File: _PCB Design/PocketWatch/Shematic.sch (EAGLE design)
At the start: 57 parts, among them Q1 MMBTA56-SOT23, U2 ATTINY88-AU

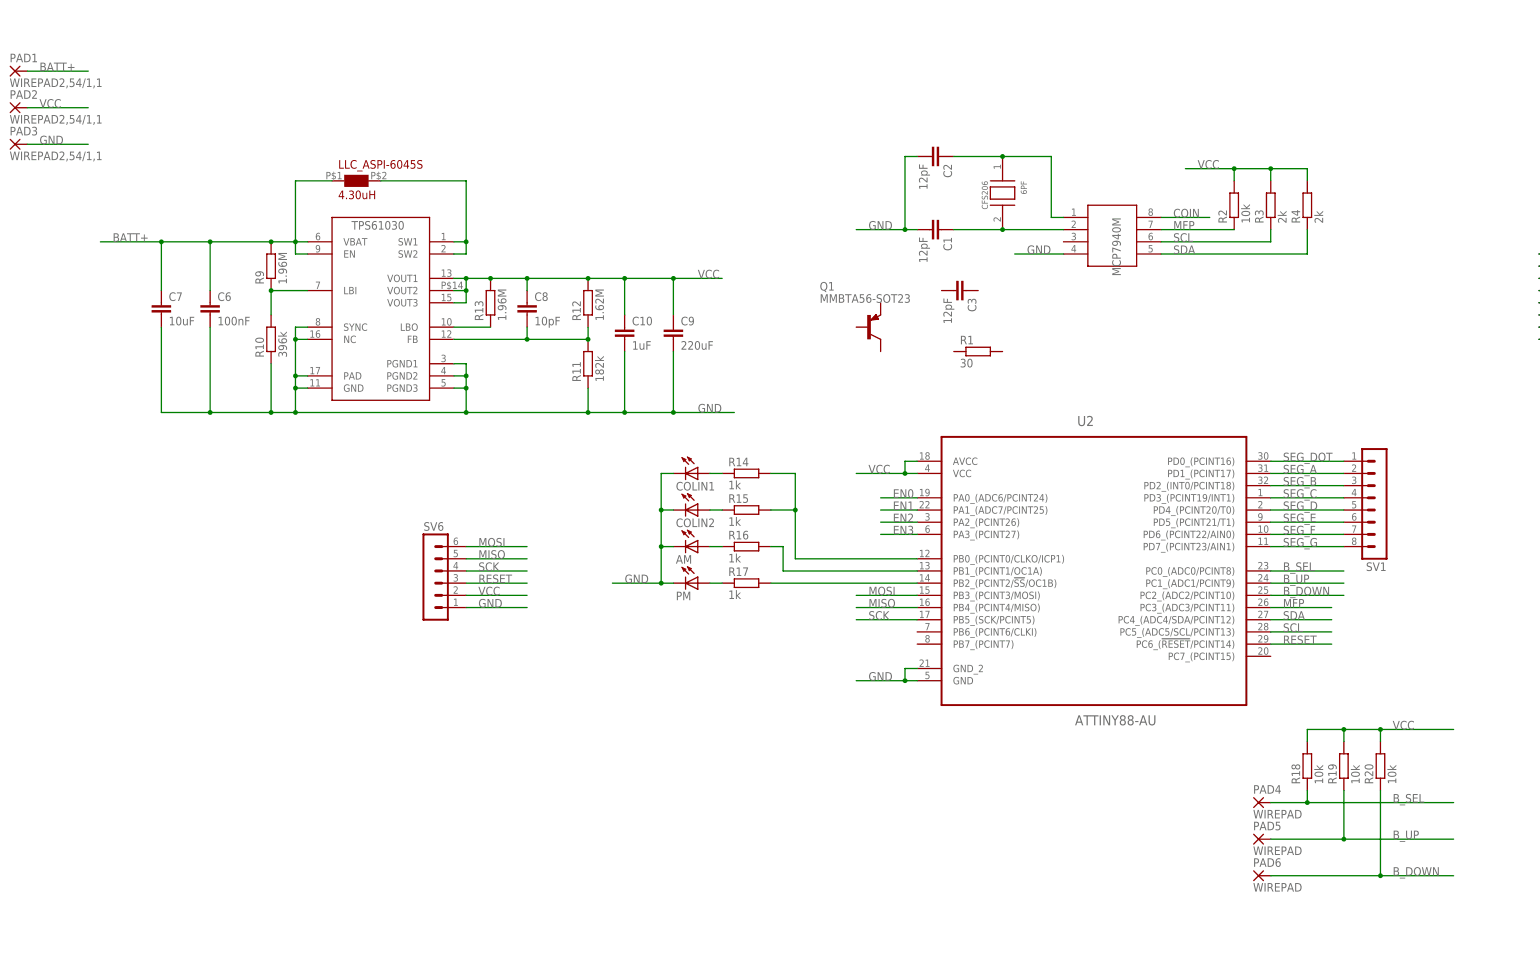
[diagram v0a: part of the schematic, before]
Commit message: Added Coin Cell
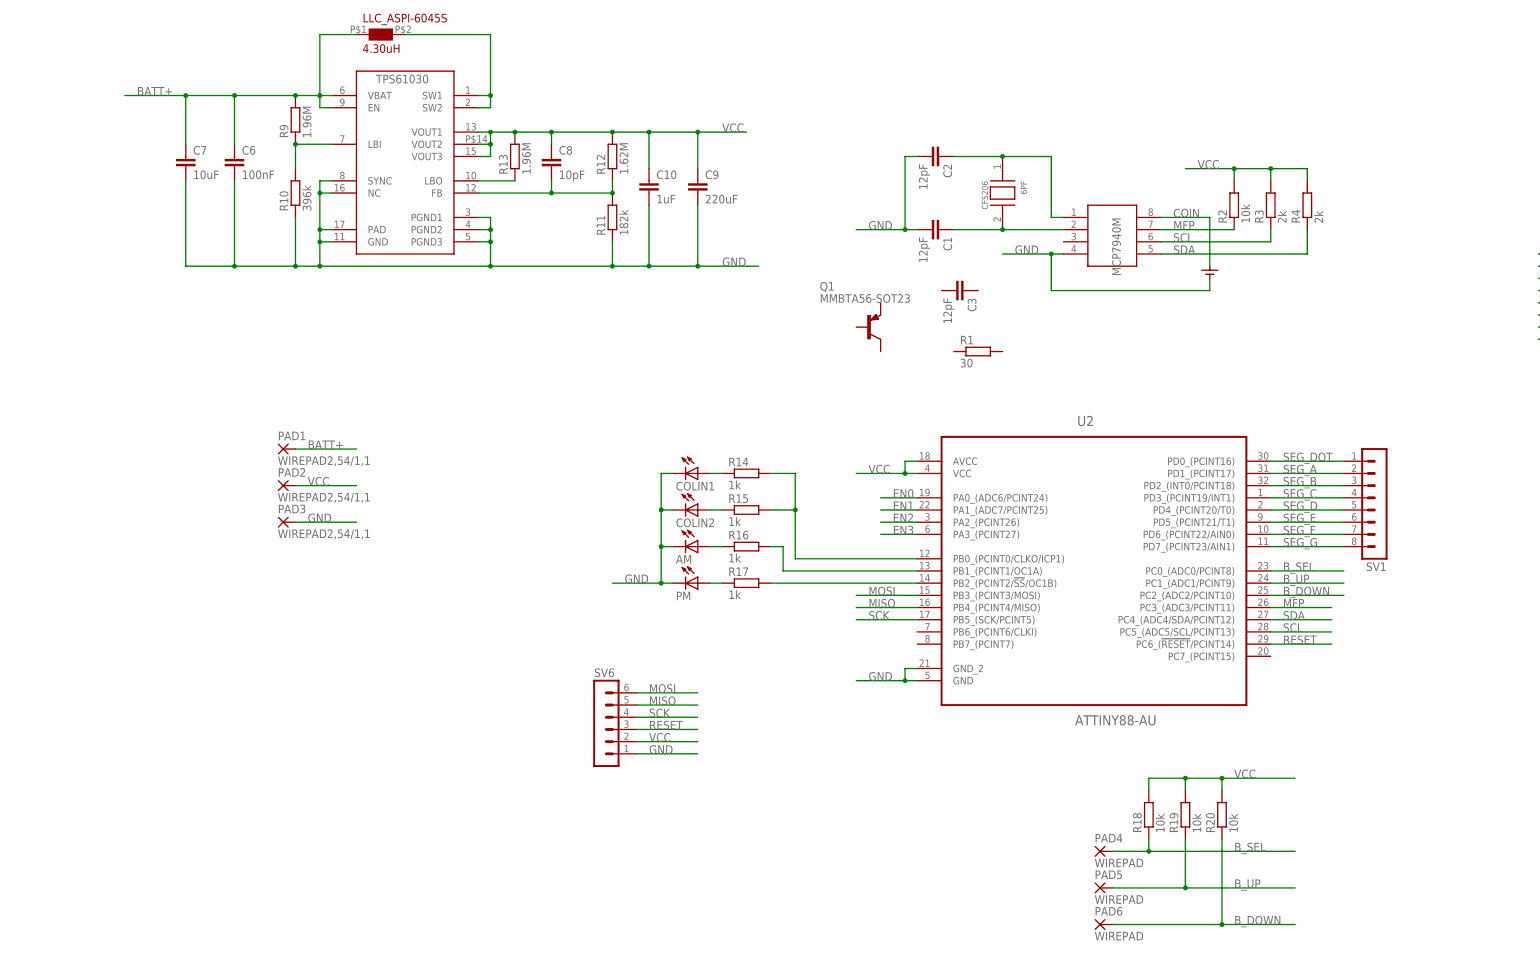
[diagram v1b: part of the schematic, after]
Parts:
- added U$5: COIN, Library:COIN
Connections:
- net COIN: now also U$5.V+
- net GND: now also U$5.V-
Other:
- moved on the sheet: C10, C6, C7, C8, C9, LLC_ASPI-6045S, PAD1, PAD2, PAD3, PAD4, PAD5, PAD6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

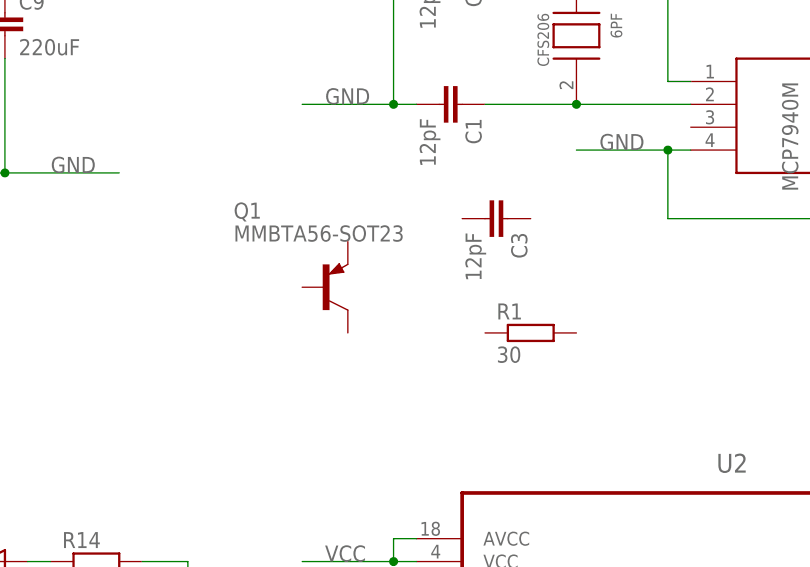
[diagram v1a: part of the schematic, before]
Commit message: Added board. Routed tubes sub-board. Fixed remaining schematic issues.
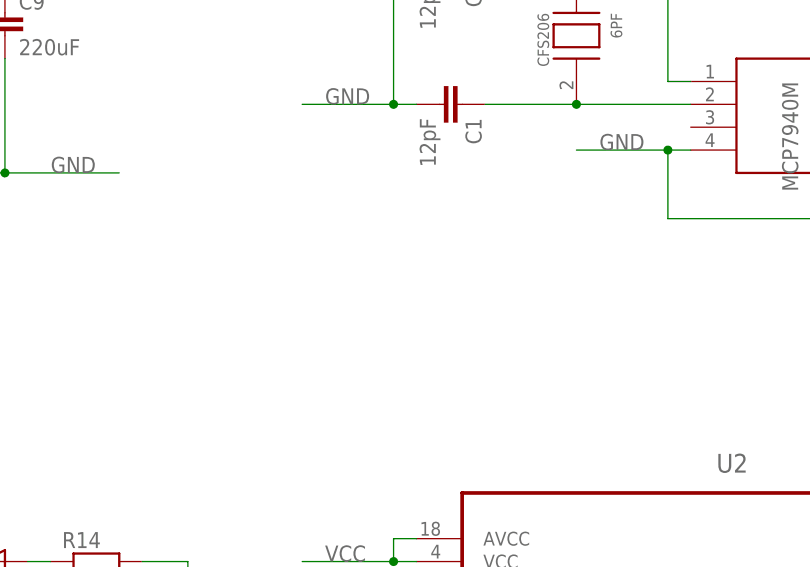
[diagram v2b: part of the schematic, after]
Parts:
- removed C3: 12pF, eagle-ltspice:CC1206
- removed Q1: MMBTA56-SOT23, transistor-pnp:MMBTA56-SOT23
- removed R1: 30, eagle-ltspice:RR1206
- renumbered U$1 to TUBE3, U$2 to TUBE2, U$3 to TUBE0, U$4 to TUBE1

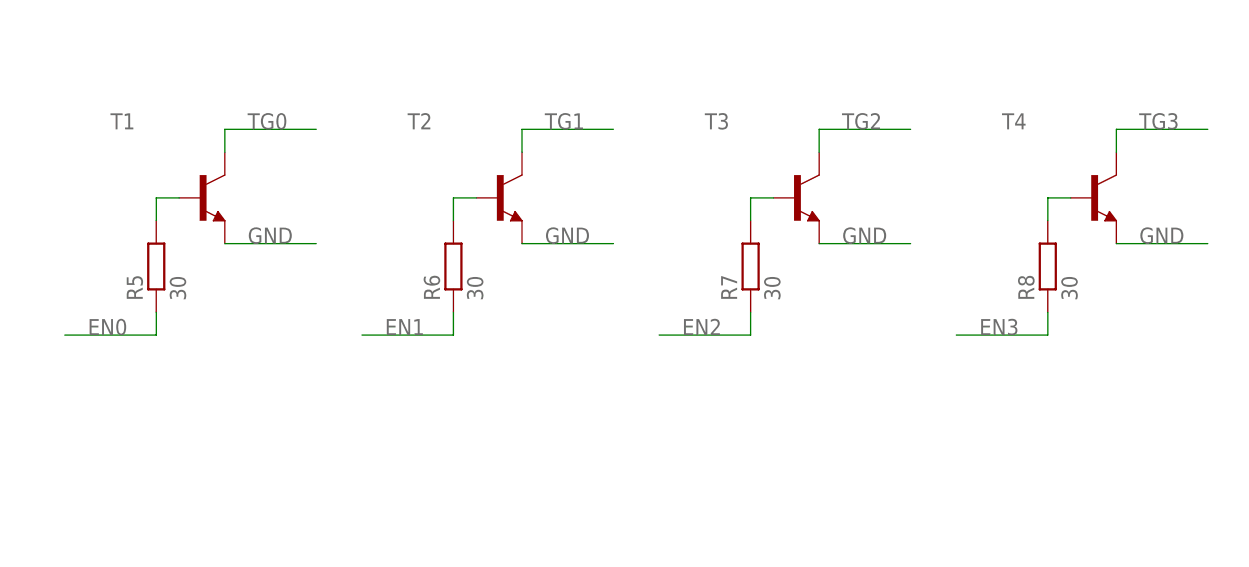
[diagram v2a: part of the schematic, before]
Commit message: Begin placement of main board. Swapped LEDs for through hole
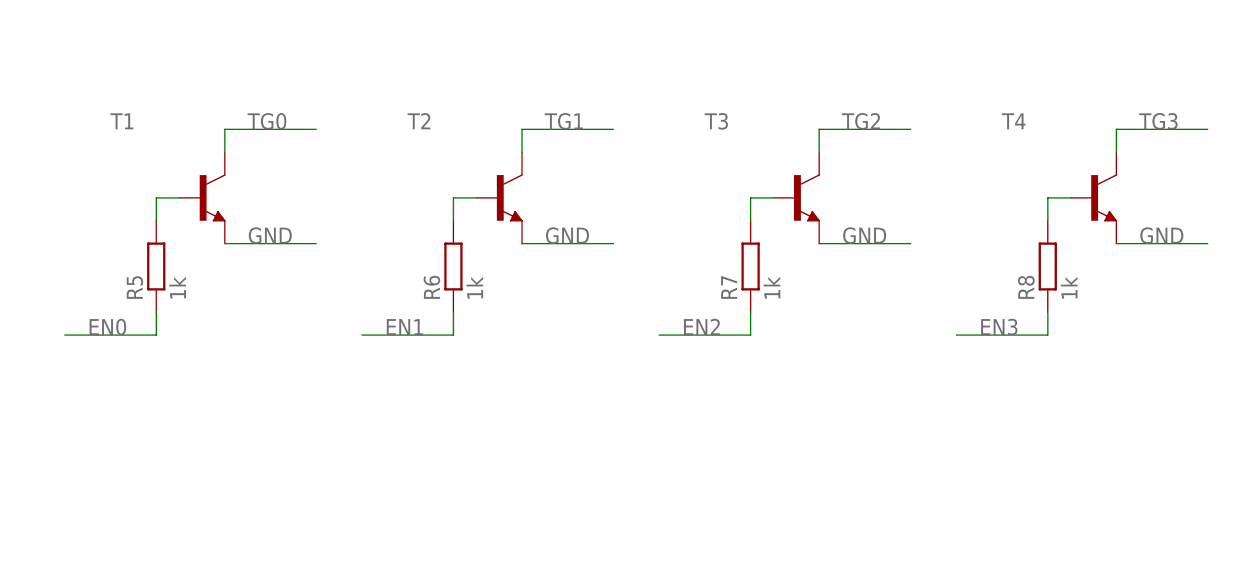
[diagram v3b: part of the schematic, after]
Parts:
- AM, COLIN1, COLIN2, PM: device eagle-ltspice:LED_E -> eagle-ltspice:LED_ELD260
- R5, R6, R7, R8: value 30 -> 1k
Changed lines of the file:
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@@
 <part name="SV5" library="con-lstb" library_urn="urn:adsk.eagle:library:162" deviceset="MA04-1" device="" package3d_urn="urn:adsk.eagle:package:8337/1"/>
 <part name="SV6" library="con-lstb" library_urn="urn:adsk.eagle:library:162" deviceset="MA06-1" device="" package3d_urn="urn:adsk.eagle:package:8340/1"/>
-<part name="R5" library="eagle-ltspice" library_urn="urn:adsk.eagle:library:217" deviceset="R" device="R1206" package3d_urn="urn:adsk.eagle:package:13301/1" value="30"/>
-<part name="R6" library="eagle-ltspice" library_urn="urn:adsk.eagle:library:217" deviceset="R" device="R1206" package3d_urn="urn:adsk.eagle:package:13301/1" value="30"/>
-<part name="R7" library="eagle-ltspice" library_urn="urn:adsk.eagle:library:217" deviceset="R" device="R1206" package3d_urn="urn:adsk.eagle:package:13301/1" value="30"/>
-<part name="R8" library="eagle-ltspice" library_urn="urn:adsk.eagle:library:217" deviceset="R" device="R1206" package3d_urn="urn:adsk.eagle:package:13301/1" value="30"/>
+<part name="R5" library="eagle-ltspice" library_urn="urn:adsk.eagle:library:217" deviceset="R" device="R1206" package3d_urn="urn:adsk.eagle:package:13301/1" value="1k"/>
+<part name="R6" library="eagle-ltspice" library_urn="urn:adsk.eagle:library:217" deviceset="R" device="R1206" package3d_urn="urn:adsk.eagle:package:13301/1" value="1k"/>
+<part name="R7" library="eagle-ltspice" library_urn="urn:adsk.eagle:library:217" deviceset="R" device="R1206" package3d_urn="urn:adsk.eagle:package:13301/1" value="1k"/>
+<part name="R8" library="eagle-ltspice" library_urn="urn:adsk.eagle:library:217" deviceset="R" device="R1206" package3d_urn="urn:adsk.eagle:package:13301/1" value="1k"/>
 <part name="C6" library="eagle-ltspice" library_urn="urn:adsk.eagle:library:217" deviceset="C" device="C1206" package3d_urn="urn:adsk.eagle:package:13279/1" value="100nF"/>
 <part name="C7" library="eagle-ltspice" library_urn="urn:adsk.eagle:library:217" deviceset="C" device="C1206" package3d_urn="urn:adsk.eagle:package:13279/1" value="10uF"/>
@@
 <part name="PAD2" library="wirepad" library_urn="urn:adsk.eagle:library:412" deviceset="WIREPAD" device="2,54/1,1" package3d_urn="urn:adsk.eagle:package:30836/1"/>
 <part name="PAD3" library="wirepad" library_urn="urn:adsk.eagle:library:412" deviceset="WIREPAD" device="2,54/1,1" package3d_urn="urn:adsk.eagle:package:30836/1"/>
-<part name="COLIN2" library="eagle-ltspice" library_urn="urn:adsk.eagle:library:217" deviceset="LED_E" device="" package3d_urn="urn:adsk.eagle:package:13319/1"/>
+<part name="COLIN2" library="eagle-ltspice" library_urn="urn:adsk.eagle:library:217" deviceset="LED_E" device="LD260" package3d_urn="urn:adsk.eagle:package:13313/1"/>
 <part name="PAD4" library="wirepad" library_urn="urn:adsk.eagle:library:412" deviceset="WIREPAD" device="2,54/1,1" package3d_urn="urn:adsk.eagle:package:30836/1" value="WIREPAD"/>
 <part name="PAD5" library="wirepad" library_urn="urn:adsk.eagle:library:412" deviceset="WIREPAD" device="2,54/1,1" package3d_urn="urn:adsk.eagle:package:30836/1" value="WIREPAD"/>
 <part name="PAD6" library="wirepad" library_urn="urn:adsk.eagle:library:412" deviceset="WIREPAD" device="2,54/1,1" package3d_urn="urn:adsk.eagle:package:30836/1" value="WIREPAD"/>
-<part name="AM" library="eagle-ltspice" library_urn="urn:adsk.eagle:library:217" deviceset="LED_E" device="" package3d_urn="urn:adsk.eagle:package:13319/1"/>
-<part name="PM" library="eagle-ltspice" library_urn="urn:adsk.eagle:library:217" deviceset="LED_E" device="" package3d_urn="urn:adsk.eagle:package:13319/1"/>
-<part name="COLIN1" library="eagle-ltspice" library_urn="urn:adsk.eagle:library:217" deviceset="LED_E" device="" package3d_urn="urn:adsk.eagle:package:13319/1"/>
+<part name="AM" library="eagle-ltspice" library_urn="urn:adsk.eagle:library:217" deviceset="LED_E" device="LD260" package3d_urn="urn:adsk.eagle:package:13313/1"/>
+<part name="PM" library="eagle-ltspice" library_urn="urn:adsk.eagle:library:217" deviceset="LED_E" device="LD260" package3d_urn="urn:adsk.eagle:package:13313/1"/>
+<part name="COLIN1" library="eagle-ltspice" library_urn="urn:adsk.eagle:library:217" deviceset="LED_E" device="LD260" package3d_urn="urn:adsk.eagle:package:13313/1"/>
 <part name="R14" library="eagle-ltspice" library_urn="urn:adsk.eagle:library:217" deviceset="R" device="R1206" package3d_urn="urn:adsk.eagle:package:13301/1" value="1k"/>
 <part name="R15" library="eagle-ltspice" library_urn="urn:adsk.eagle:library:217" deviceset="R" device="R1206" package3d_urn="urn:adsk.eagle:package:13301/1" value="1k"/>
